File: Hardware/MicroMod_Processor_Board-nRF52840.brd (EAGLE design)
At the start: 22 x 22 mm, 40 parts, among them J1 MICROMOD-2222, U1 ARTEMIS_MODULESMD, U2 TSV524, U6 CH340E_MSOP10, Y1 32.768kHz

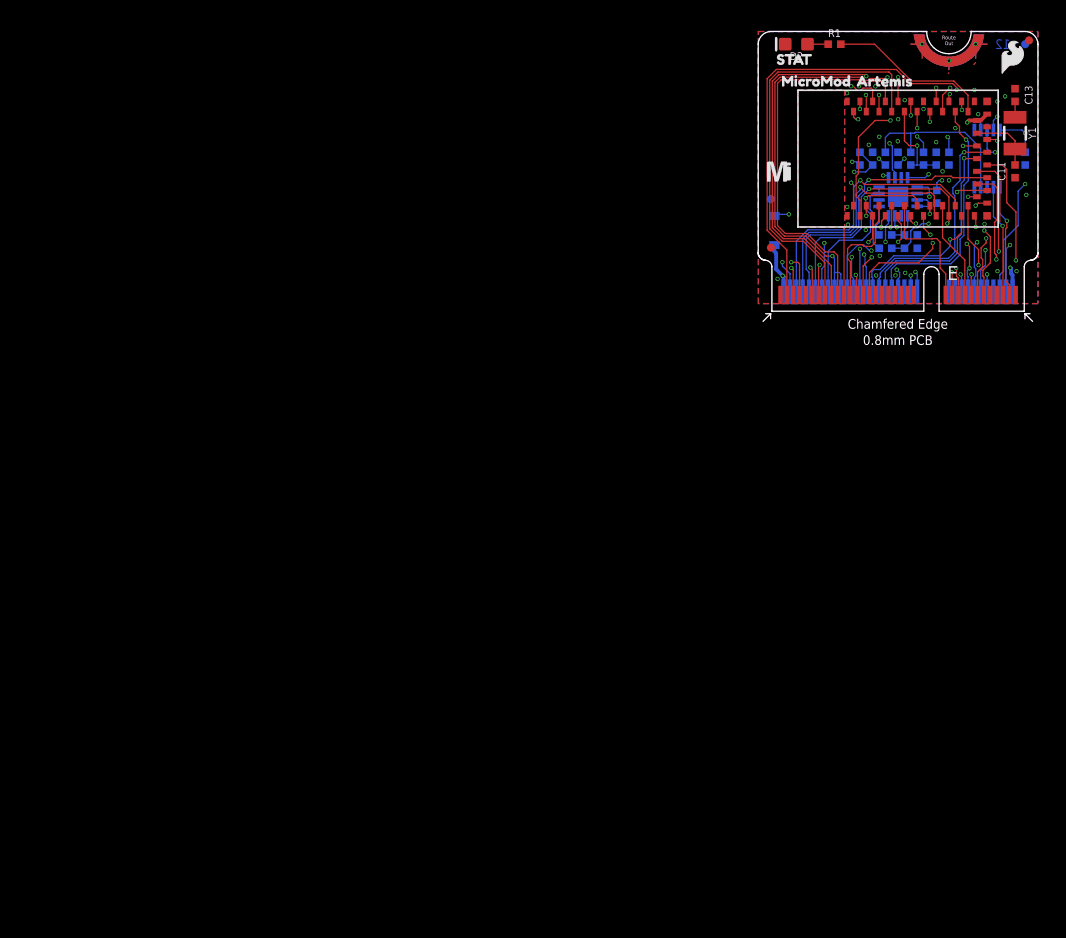
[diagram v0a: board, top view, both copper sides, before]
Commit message: Renamed eagle files appropriately
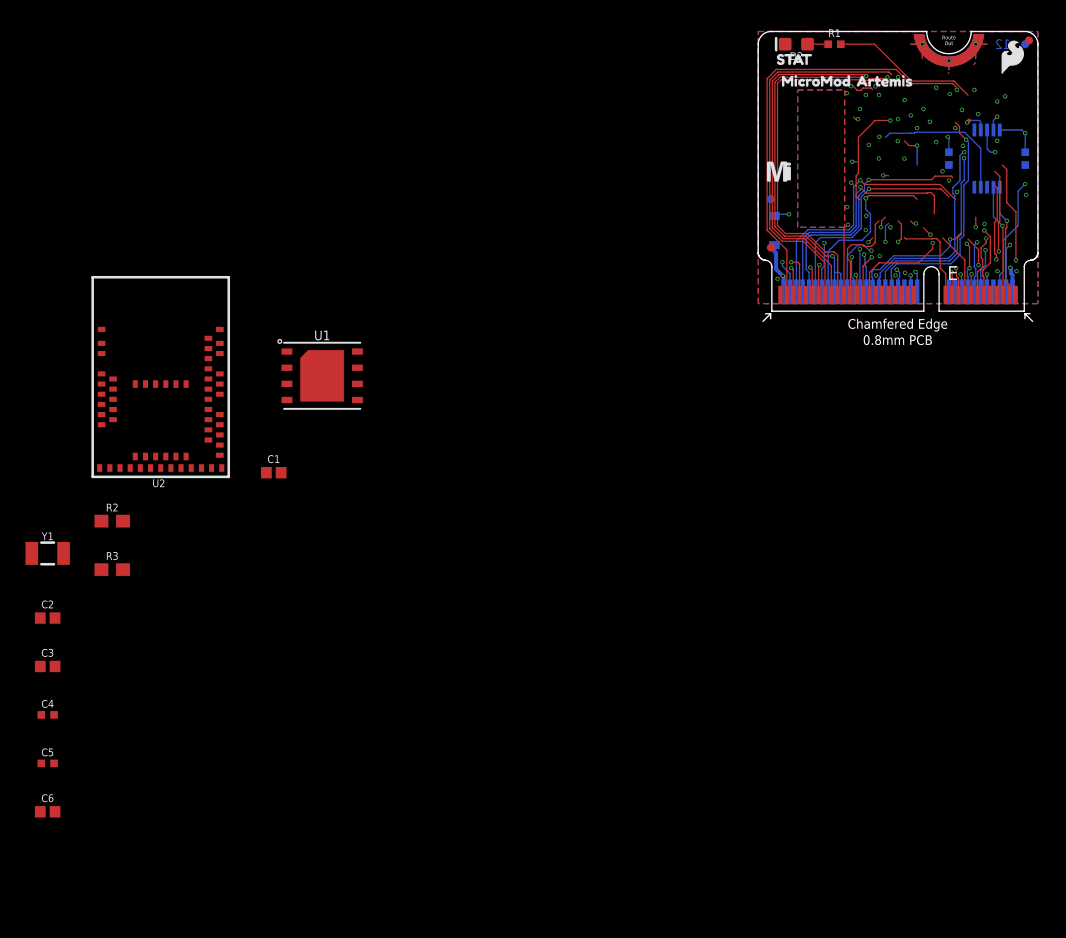
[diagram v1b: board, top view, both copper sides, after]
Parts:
- removed C11, C13: 15pF, SparkFun-Capacitors:0402-TIGHT
- removed C20, C21: 0.1uF, SparkFun-Capacitors:0402-TIGHT
- removed C28: 1.0nF, SparkFun-Capacitors:0402-TIGHT
- removed R14, R6: 100k, SparkFun-Resistors:0402-TIGHT
- removed R15: 220KOHM-0402T-1/16W-1%, SparkFun-Resistors:0402-TIGHT
- removed R4, R5, R7: 150k, SparkFun-Resistors:0402-TIGHT
- added C2, C3: 15pF, SparkFun-Capacitors:0402
- added C4, C5: 10uF, SparkFun-Capacitors:0402-TIGHT
- added C6: 0.1uF, SparkFun-Capacitors:0402
- C1: device SparkFun-Capacitors:0402-TIGHT -> SparkFun-Capacitors:0402
- R2, R3: value 100k -> 27; device SparkFun-Resistors:0402-TIGHT -> SparkFun-Resistors:0603
- U1: value ARTEMIS_MODULESMD -> W25QXX128MBIT-6X5; device SparkFun-IC-Microcontroller:ARTEMIS_FP -> SparkFun-MicroMod:WSON-8-6X5
- U2: value TSV524 -> MDBT50Q; device OpAmp:QFN-16 -> nrf52840:MDBT50Q
- moved Y1 82.9 mm to (-55.9, -19.1), turned to 0 degrees
- moved R3 65.9 mm to (-50.8, -20.3), flipped to the top
- moved R2 65.3 mm to (-50.8, -16.5), flipped to the top, turned to 0 degrees
- moved U2 59.7 mm to (-47.0, -5.08), flipped to the top, turned to 0 degrees
- moved C1 56.5 mm to (-38.1, -12.7), flipped to the top, turned to 0 degrees
- moved U1 48.9 mm to (-34.3, -5.08), turned to 0 degrees
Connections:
- removed net ADC0_BUFF1: R3.2, U2.15, U2.16
- removed net ADC0_BUFF2: R3.1, R5.2, U2.4
- removed net ADC1_BUFF2: R6.1, R7.2, U2.9
- removed net ADC_BUFF1: R6.2, U2.13, U2.14
- removed net N$7: C11.2, U1.XO, Y1.P$2
- removed net SCALED_ADC0: U1.~AD32, U2.5, U2.6
- removed net SCALED_ADC1: U1.~AD35, U2.7, U2.8
- removed net SCALED_BATT_VIN/3: R2.1, R4.2, U1.~AD31
- new net N$1: R2.2, U2.35
- new net N$3: R3.2, U2.34
- net !RESET!: no longer C20.2, C28.1, R14.1, U1.~RST
- net !RTS: no longer C20.1, C21.1
- net 3.3V: now also C4.1, C5.1, C6.1, U1.8, U2.28, U2.30; no longer R14.2, U1.VDD@36, U1.VDD@37, U2.2
- net 3.3V_EN: no longer U1.D3
- net ADC0: no longer U2.1
- net ADC1: no longer U2.12
- net ADC_D+: no longer U1.~AD13
- net ADC_D-: no longer U1.~AD12
- net BATT_VIN/3: no longer R2.2
- net BOOT: no longer C21.2, R15.2, U1.BOOT
- net CAM_PCLK: no longer U1.~AD11
- net CLKOUT: no longer U1.D0
- net CTS1: no longer U1.D17
- net D0: no longer U1.D1
- net D1: no longer U1.D2
- net GND: now also C2.1, C3.1, C4.2, C5.2, C6.2, U1.4, U2.1, U2.15, U2.2, U2.33, U2.55; no longer C11.1, C13.1, C28.2, R15.1, R4.1, R5.1, R7.1, U1.GND@1, U1.GND@22, U1.GND@38, U1.GND@39, U1.GND@47, U1.GND@59, U2.11
- net GPIO0: no longer U1.AD16
- net GPIO1: no longer U1.~AD33/SWO
- net GPIO2: no longer U1.AD34
- net GPIO3: no longer U1.~D27
- net GPIO4: no longer U1.~D28
- net GPIO5: no longer U1.~AD29
- net GPIO6: no longer U1.D14
- net GPIO7: no longer U1.D15
- net I2C_!INT!: no longer U1.~D18
- net LED_BUILTIN: no longer U1.~D19
- net N$4: now also C3.2, U2.17, Y1.P$1; no longer U1.XI
- net N$5: now also C2.2, U2.18, Y1.P$2; no longer C13.2, Y1.P$1
- net PDM_CLK: no longer U1.~D37
- net PDM_DATA: no longer U1.D36
- net PWM0: no longer U1.~D44
- net PWM1: no longer U1.~D45
- net RTS1: no longer U1.D10
- net RX1: no longer U1.~D25
- net RXI-0: no longer U1.RXI-0
- net SCL: no longer U1.~D39
- net SCL1: no longer U1.D8
- net SDA: no longer U1.D40
- net SDA1: no longer U1.D9
- net SDIO_DATA1: no longer U1.~D26
- net SDIO_DATA2: no longer U1.~D4
- net SPI_!CS!: no longer U1.~D23
- net SPI_!CS!1: no longer U1.D41
- net SPI_MISO: no longer U1.~D22, U1.~D6
- net SPI_MISO1: no longer U1.~D43
- net SPI_MOSI: no longer U1.D7
- net SPI_MOSI1: no longer U1.D38
- net SPI_SCK: no longer U1.~D5
- net SPI_SCK1: no longer U1.~D42
- net SWDCK: now also U2.53; no longer U1.SWDCK
- net SWDIO: now also U2.51; no longer U1.SWDIO
- net TX1: no longer U1.~D24
- net TXO-0: no longer U1.TXO-0
- net USB_D+: now also R2.1
- net USB_D-: now also R3.1
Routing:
- net SCALED_BATT_VIN/3: track 19.8 -> 0.00 mm, vias 3 -> 0
- net ADC0_BUFF2: track 10.3 -> 0.00 mm, vias 2 -> 0
- net 3.3V: track 17.7 -> 10.7 mm, vias 8 -> 5
- net SPI_MISO: track 24.4 -> 17.8 mm, vias 3 -> 1
- net SCALED_ADC0: track 6.35 -> 0.00 mm, vias 2 -> 0
- net ADC0_BUFF1: track 5.69 -> 0.00 mm
- net N$7: track 5.15 -> 0.00 mm
- net !RESET!: track 26.0 -> 21.7 mm
- net SCALED_ADC1: track 3.61 -> 0.00 mm, vias 1 -> 0
- net ADC_BUFF1: track 2.95 -> 0.00 mm
- net SPI_MISO1: track 32.5 -> 29.6 mm
- net SDIO_DATA1: track 22.3 -> 19.6 mm
- net !RTS: track 13.9 -> 11.3 mm
- net GPIO6: track 22.9 -> 20.2 mm
- net ADC1_BUFF2: track 2.60 -> 0.00 mm
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
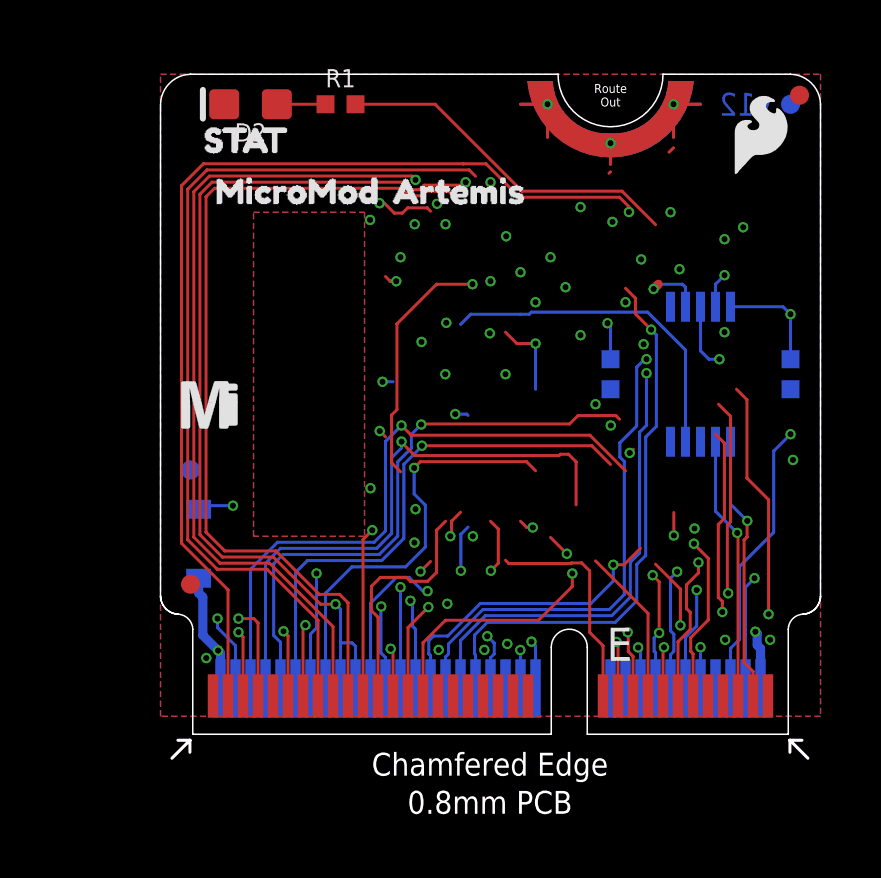
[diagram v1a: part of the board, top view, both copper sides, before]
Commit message: Ripped up old traces
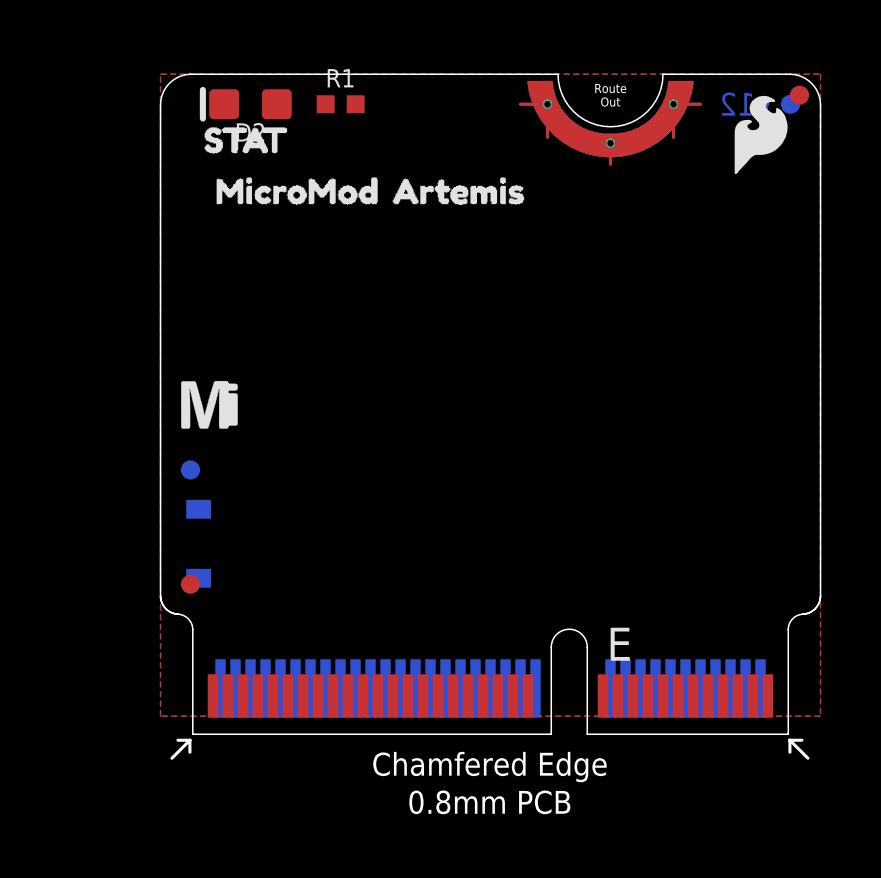
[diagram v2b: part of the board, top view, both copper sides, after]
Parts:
- removed C17: 10nF, SparkFun-Capacitors:0402-TIGHT
- removed C18: 0.1uF, SparkFun-Capacitors:0402-TIGHT
- removed U6: CH340E_MSOP10, SparkFun-IC-Comms:MSOP10
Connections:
- removed net !RTS: U6.4
- removed net RXI-0: U6.8
- removed net TXO-0: U6.9
- net 3.3V: no longer C17.1, C18.1, U6.10, U6.7
- net GND: no longer C17.2, C18.2, U6.3
- net USB_D+: no longer U6.1
- net USB_D-: no longer U6.2
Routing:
- net GPIO5: track 41.0 -> 7.22 mm, vias 2 -> 0
- net CLKOUT: track 31.7 -> 0.83 mm, vias 3 -> 0
- net SPI_MISO1: track 29.6 -> 0.00 mm
- net SPI_SCK1: track 28.9 -> 0.00 mm
- net SPI_MOSI1: track 28.9 -> 1.49 mm, vias 2 -> 0
- net TXO-0: track 21.0 -> 0.00 mm, vias 3 -> 0
- net SPI_!CS!: track 20.8 -> 0.00 mm, vias 1 -> 0
- net RXI-0: track 20.0 -> 0.00 mm, vias 2 -> 0
- net SDIO_DATA1: track 19.6 -> 0.00 mm, vias 1 -> 0
- net SDIO_DATA2: track 19.6 -> 0.00 mm, vias 1 -> 0
- net GPIO0: track 18.8 -> 0.00 mm, vias 1 -> 0
- net SPI_MISO: track 17.8 -> 0.00 mm, vias 1 -> 0
- net GPIO2: track 16.4 -> 0.00 mm, vias 1 -> 0
- net GPIO1: track 15.6 -> 0.00 mm, vias 1 -> 0
- net SPI_SCK: track 14.2 -> 0.00 mm, vias 1 -> 0
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
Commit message: Removed some dividing lines in schematic
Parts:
- removed U$6: (no value), buzzard_labels (1):ARTEMIS2
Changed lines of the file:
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@@
 <element name="U$2" library="buzzard_labels" package="ARTEMIS0" value="" x="7" y="18.1" smashed="yes"/>
 <element name="U$3" library="buzzard_labels" package="MICROMOD1" value="" x="1.1" y="18.1" smashed="yes"/>
-<element name="U$6" library="buzzard_labels (1)" package="ARTEMIS2" value="" x="14.3" y="13.7" smashed="yes" rot="MR0"/>
 <element name="LOGO3" library="SparkFun-Aesthetics" package="OSHW-LOGO-MINI" value="OSHW-LOGOMINI" x="2" y="20" smashed="yes" rot="MR0"/>
 <element name="LOGO4" library="SparkFun-Aesthetics" package="ORDERING_INSTRUCTIONS" value="SPECIAL_INSTRUCTIONS-ORDERING" x="24.54" y="50.8" smashed="yes"/>
@@
 <wire x1="-51.64" y1="-2.53" x2="-51.64" y2="-1.43" width="0" layer="19" extent="1-1"/>
 <wire x1="1.75" y1="1.275" x2="-37.065" y2="-6.985" width="0" layer="19" extent="1-1"/>
-<wire x1="9.25" y1="1.275" x2="1.75" y2="1.275" width="0" layer="19" extent="1-1"/>
-<wire x1="10.75" y1="1.275" x2="9.25" y2="1.275" width="0" layer="19" extent="1-1"/>
-<wire x1="11.5" y1="1.525" x2="10.75" y2="1.275" width="0" layer="19" extent="1-16"/>
-<wire x1="12.25" y1="1.275" x2="11.5" y2="1.525" width="0" layer="19" extent="1-16"/>
-<wire x1="18.75" y1="1.275" x2="12.25" y2="1.275" width="0" layer="19" extent="1-1"/>
-<wire x1="20.25" y1="1.275" x2="18.75" y2="1.275" width="0" layer="19" extent="1-1"/>
-<wire x1="15" y1="19.7" x2="11.5" y2="1.525" width="0" layer="19" extent="16-16"/>
-<wire x1="17.1" y1="21" x2="15" y2="19.7" width="0" layer="19" extent="1-1"/>
-<wire x1="12.9" y1="21" x2="15" y2="19.7" width="0" layer="19" extent="1-1"/>
-<wire x1="2.123" y1="21" x2="12.9" y2="21" width="0" layer="19" extent="1-1"/>
 </signal>
 <signal name="!RESET!">

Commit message: Determined nets of some nRF pins.
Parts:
- removed U$2: (no value), buzzard_labels:ARTEMIS0
- moved U2 60.7 mm to (11.4, 11.4), turned to 90 degrees
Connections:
- new net NFC1: J1.43, U2.52
- new net NFC2: J1.41, U2.54
- new net RX2: J1.20, U2.42
- new net TX2: J1.22, U2.44
- net GPIO0: now also U2.57
- net GPIO1: now also U2.58
- net GPIO2: now also U2.25
- net GPIO3: now also U2.26
- net GPIO4: now also U2.3
- net GPIO5: now also U2.4
- net GPIO6: now also U2.5
- net GPIO7: now also U2.6
- net LED_BUILTIN: now also U2.23
- net RX1: now also U2.39
- net SCL: now also U2.27
- net SDA: now also U2.24
- net SDIO_DATA1: now also U2.60
- net SDIO_DATA2: now also U2.56
- net SPI_!CS!: now also U2.59
- net SPI_MISO: now also U2.50
- net SPI_MISO1: now also U2.12
- net SPI_MOSI: now also U2.61
- net SPI_MOSI1: now also U2.9
- net SPI_SCK: now also U2.47
- net SPI_SCK1: now also U2.14
- net TX1: now also U2.41
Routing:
- net 3.3V_EN: track 22.0 -> 0.00 mm
- net 3.3V_MAIN: track 20.3 -> 0.00 mm
- net GPIO7: track 18.8 -> 0.00 mm
- net SPI_!CS!1: track 18.6 -> 0.00 mm
- net D0: track 18.4 -> 0.00 mm
- net PWM0: track 18.1 -> 0.00 mm
- net CAM_PCLK: track 16.4 -> 0.00 mm
- net BOOT: track 16.2 -> 0.00 mm
- net SWDCK: track 15.9 -> 0.00 mm
- net CTS1: track 15.9 -> 0.00 mm
- net GPIO6: track 15.7 -> 0.00 mm
- net ADC_D-: track 15.4 -> 0.00 mm
- net ADC_D+: track 14.8 -> 0.00 mm
- net D1: track 14.7 -> 0.00 mm
- net SCL: track 14.3 -> 0.00 mm
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- removed copper zone on layer 15, net GND

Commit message: Working on schematic
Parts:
- removed D7: 1A/23V/620mV, SparkFun-DiscreteSemi:SOD-323
- removed J1: MICROMOD-2222, SparkFun-MicroMod:M.2-CARD-E-22
- added J2: MICROMOD-2222, SparkFun-MicroMod:M.2-CARD-E-22
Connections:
- removed net 3.3V_MAIN: D7.A, J1.2, J1.74
- removed net CAM_PCLK: J1.54
- removed net CLKOUT: J1.56, J1.58
- new net N$6: U1.1
- new net USB_VIN: J2.9, U2.32
- net !RESET!: now also J2.6; no longer J1.6
- net 3.3V: now also J2.2, J2.74; no longer D7.C, J1.72
- net 3.3V_EN: now also J2.4; no longer J1.4
- net ADC0: now also J2.34, U2.20; no longer J1.34
- net ADC1: now also J2.38, U2.21; no longer J1.38
- net ADC_D+: now also J2.63, U2.13; no longer J1.63
- net ADC_D-: now also J2.65, U2.11; no longer J1.65
- net BATT_VIN/3: now also J2.49, U2.10; no longer J1.51
- net BOOT: now also J2.11; no longer J1.11
- net CTS1: now also J2.15, U2.22; no longer J1.15
- net D0: now also J2.10, U2.16; no longer J1.10
- net D1: now also J2.18, U2.25; no longer J1.18
- net GND: now also J2.1, J2.33, J2.36, J2.39, J2.45, J2.7, J2.75, J2.GND1, J2.GND2, J2.GND3; no longer J1.1, J1.33, J1.36, J1.39, J1.45, J1.7, J1.75, J1.GND1, J1.GND2, J1.GND3
- net GPIO0: now also J2.40, U2.8; no longer J1.40, U2.57
- net GPIO1: now also J2.42, U2.7; no longer J1.42, U2.58
- net GPIO2: now also J2.44, U2.6; no longer J1.44, U2.25
- net GPIO3: now also J2.46, U2.5; no longer J1.46, U2.26
- net GPIO4: now also J2.48, U2.4; no longer J1.48, U2.3
- net GPIO5: now also J2.73, U2.3; no longer J1.73, U2.4
- net GPIO6: now also J2.71, U2.57; no longer J1.71, U2.5
- net GPIO7: now also J2.69, U2.56; no longer J1.69, U2.6
- net I2C_!INT!: now also J2.16, U2.60; no longer J1.16
- net NFC1: now also J2.43; no longer J1.43
- net NFC2: now also J2.41; no longer J1.41
- net PDM_CLK: now also J2.50, U2.49; no longer J1.50
- net PDM_DATA: now also J2.52, U2.50; no longer J1.52
- net PWM0: now also J2.32, U2.26; no longer J1.32
- net PWM1: now also J2.47, U2.38; no longer J1.47
- net RTS1: now also J2.13, U2.19; no longer J1.13
- net RX1: now also J2.19; no longer J1.19
- net RX2: now also J2.20, U2.59; no longer J1.20, U2.42
- net SCL: now also J2.14; no longer J1.14
- net SCL1: now also J2.53, U2.48; no longer J1.55
- net SDA: now also J2.12; no longer J1.12
- net SDA1: now also J2.51, U2.61; no longer J1.53
- net SDIO_DATA1: now also J2.66, U1.2, U2.46; no longer J1.66, U2.60
- net SDIO_DATA2: now also J2.68, U1.3, U2.45; no longer J1.68, U2.56
- net SPI_!CS!: now also J2.70, U1.7, U2.47; no longer J1.70, U2.59
- net SPI_!CS!1: now also J2.55, U2.44; no longer J1.49
- net SPI_MISO: now also J2.64, U1.5, U2.43; no longer J1.64, U2.50
- net SPI_MISO1: now also J2.61; no longer J1.61
- net SPI_MOSI: now also J2.62, U2.40; no longer J1.62, U2.61
- net SPI_MOSI1: now also J2.59; no longer J1.59
- net SPI_SCK: now also J2.60, U1.6, U2.42; no longer J1.60, U2.47
- net SPI_SCK1: now also J2.57; no longer J1.57
- net SWDCK: now also J2.21; no longer J1.21
- net SWDIO: now also J2.23; no longer J1.23
- net TX1: now also J2.17; no longer J1.17
- net TX2: now also J2.22, U2.58; no longer J1.22, U2.44
- net USB_D+: now also J2.3; no longer J1.3
- net USB_D-: now also J2.5; no longer J1.5
